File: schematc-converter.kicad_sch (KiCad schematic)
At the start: 52 parts, among them IC2 ACHS-7123-000E, IC3 LM5106MMX_NOPB, IC5 HCPL2531SDM, Q1 CSD19531Q5AT, Q2 CSD19531Q5AT

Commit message: Repair files
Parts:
- removed D2, D3, D4: LED, Diode_SMD:D_1206_3216Metric, symbol Device:LED
- removed R2, R3, R4: 1k, LED_SMD:LED_1206_3216Metric, symbol Device:R
- added C52: 100n, symbol Device:C
- added C53: 1n, symbol Device:C
- added IC2: ACHS-7123-000E, SOIC127P606X204-8N, symbol achs Current Hall Sensor:ACHS-7123-000E
- added R18: 10k, LED_SMD:LED_1206_3216Metric, symbol Device:R
- added R18: 20k, LED_SMD:LED_1206_3216Metric, symbol Device:R
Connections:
- net +5V: now also C52.1, IC2.8 (VDD)
- net GND: now also C52.2, C53.2, IC2.5 (GND), R18.1
- net SC+: now also IC2.1 (IP+_1), IC2.2 (IP+_2)
- net SC_c2: now also R18.2
- new net: IC2.7 (VOUT), R18.2
- new net: C53.1, IC2.6 (FILTER)
- new net MC+: IC2.3 (IP-_1), IC2.4 (IP-_2)
- new net MC_c: R18.1, R18.2
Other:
- note removed: "Signal diodes"
- moved on the sheet: C26, C37, C38, C39, C40, C41, C42, C43, C47, C48, D10, D8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

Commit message: P1
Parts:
- removed C49, C50: 15p, symbol Device:C
- removed C51: 100n, symbol Device:C
- removed IC5: HCPL2531SDM, HCPL2531SDM, symbol HCLP2530 transoptor:HCPL2531SDM
- removed R18 (x2): 10k, LED_SMD:LED_1206_3216Metric, symbol Device:R
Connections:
- net at IC3.7 (EN): now also R2.2
- net at IC3.8 (IN): now also R2.1
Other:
- note added: "Sprawdzic rezystory i wydajnosc ESP, pobor transoprtora i pobor drivera"
- note removed: "Sprawdzic rezystory i wydajnosc ESP, pobor transoprtora i pobor drivera Jakie bramki NOT?"
- moved on the sheet: R2

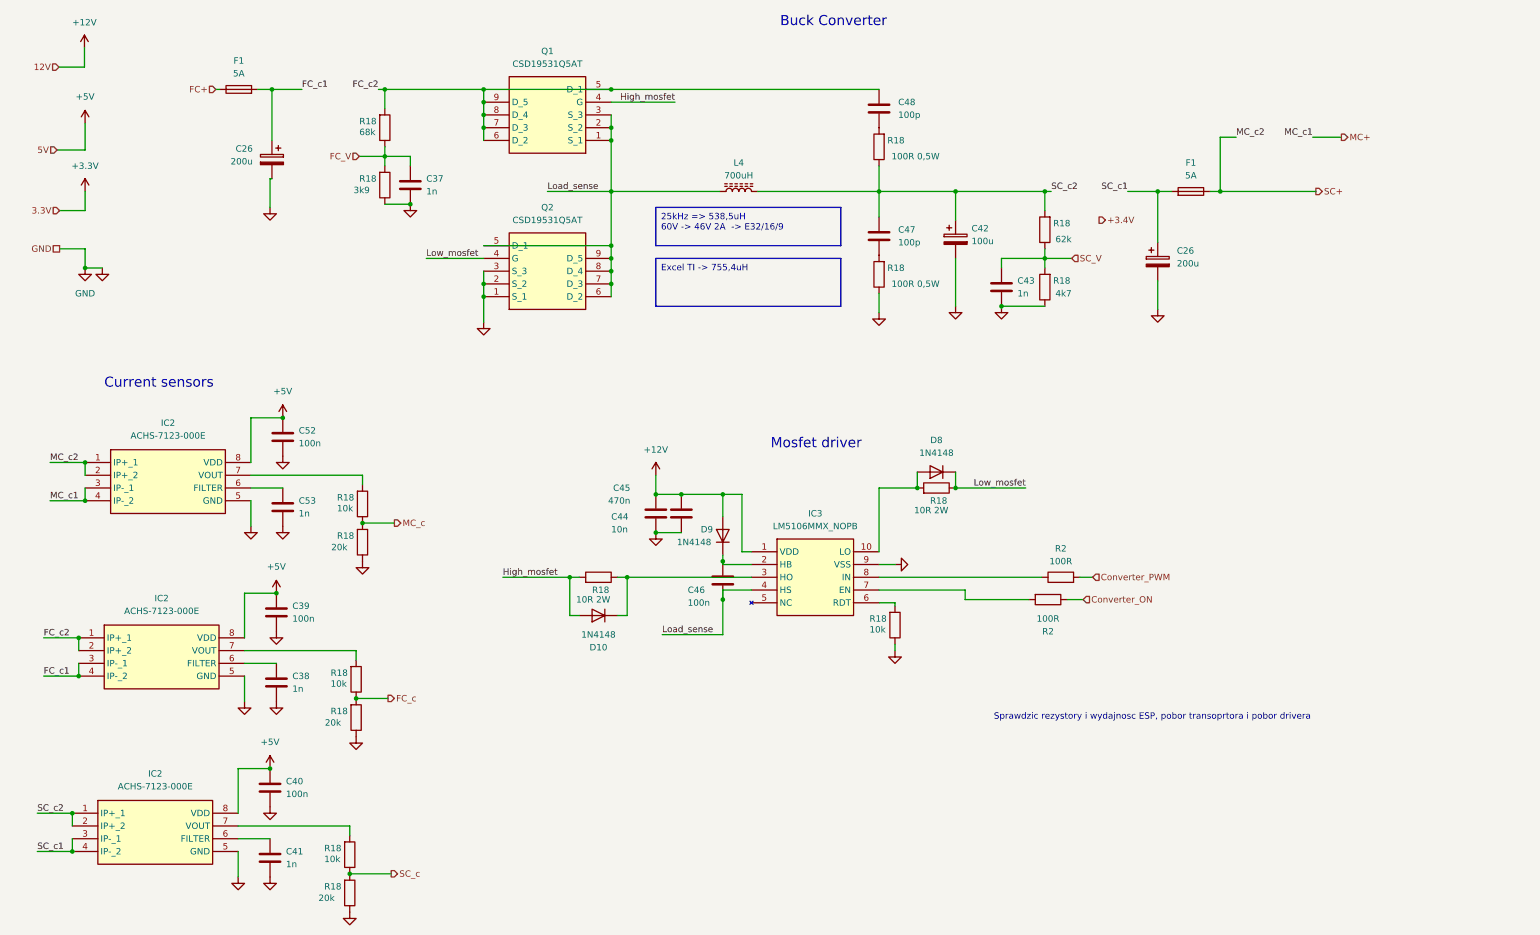
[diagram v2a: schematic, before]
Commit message: Add test points
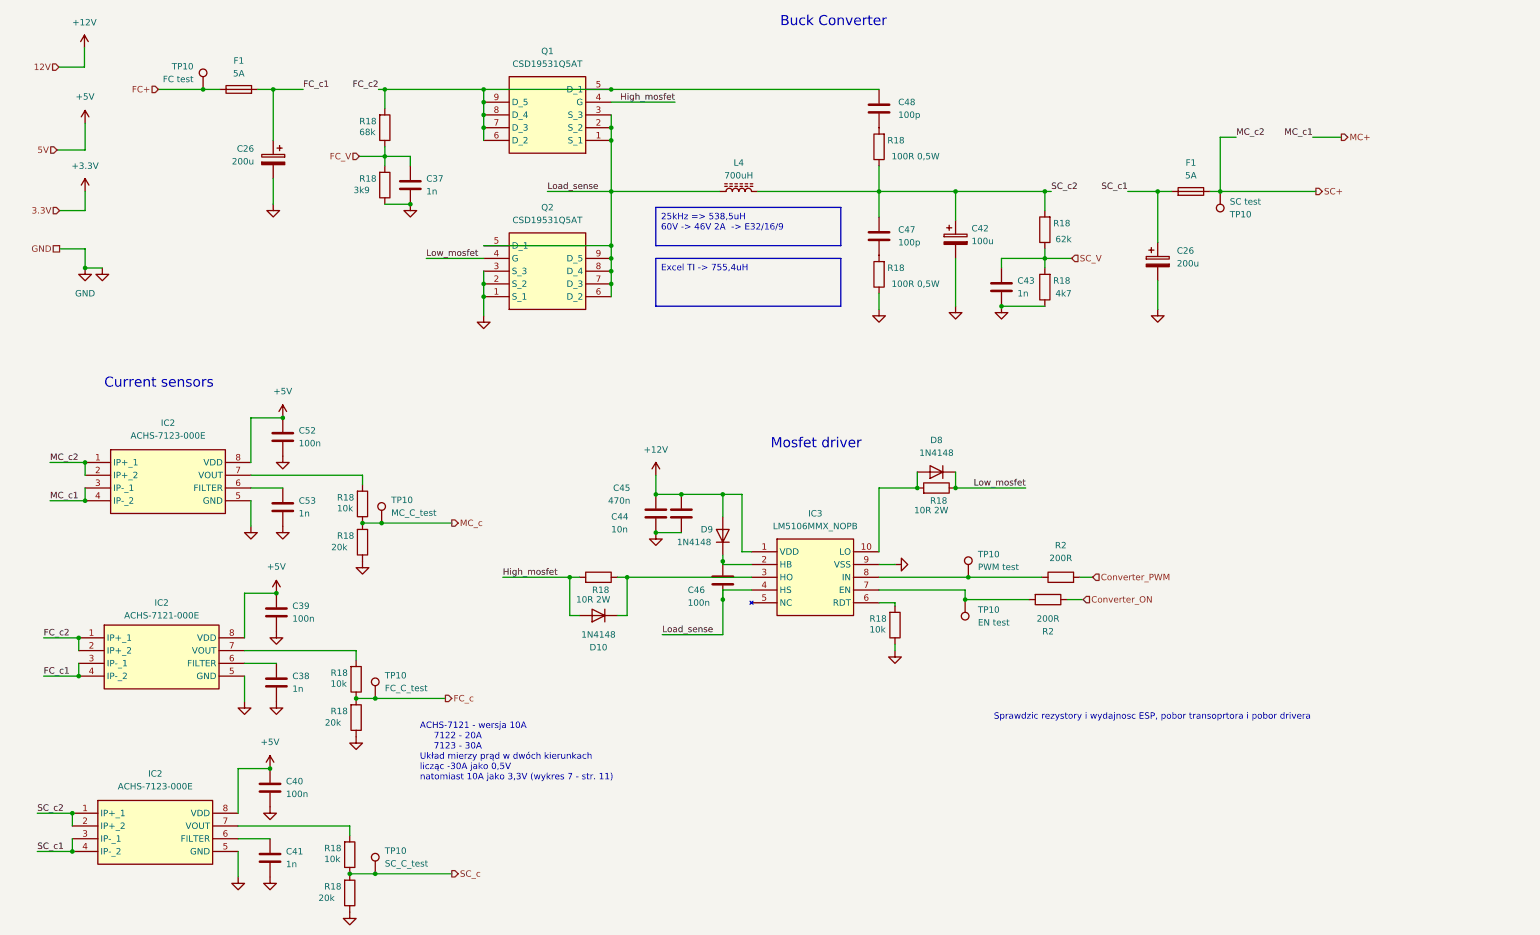
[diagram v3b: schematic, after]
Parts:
- added TP10: SC_C_test, symbol Connector:TestPoint
- added TP10: PWM test, symbol Connector:TestPoint
- added TP10: SC test, symbol Connector:TestPoint
- added TP10: EN test, symbol Connector:TestPoint
- added TP10: FC test, symbol Connector:TestPoint
- added TP10: MC_C_test, symbol Connector:TestPoint
- added TP10: FC_C_test, symbol Connector:TestPoint
- IC2: value ACHS-7123-000E -> ACHS-7121-000E
- R2: value 100R -> 200R
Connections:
- net FC+: now also TP10.1
- net FC_c: now also TP10.1
- net MC_c: now also TP10.1
- net SC+: now also TP10.1
- net SC_c: now also TP10.1
- net at IC3.7 (EN), R2.2: now also TP10.1
- net at IC3.8 (IN), R2.1: now also TP10.1
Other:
- note added: "ACHS-7121 - wersja 10A 7122 - 20A 7123 - 30A Układ mierzy prąd w dwóch kierunkach licząc -30A jako 0,5V natomiast 10A jako 3,3V (wykres 7 - str. 11)"

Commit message: Edit mosfets outputs
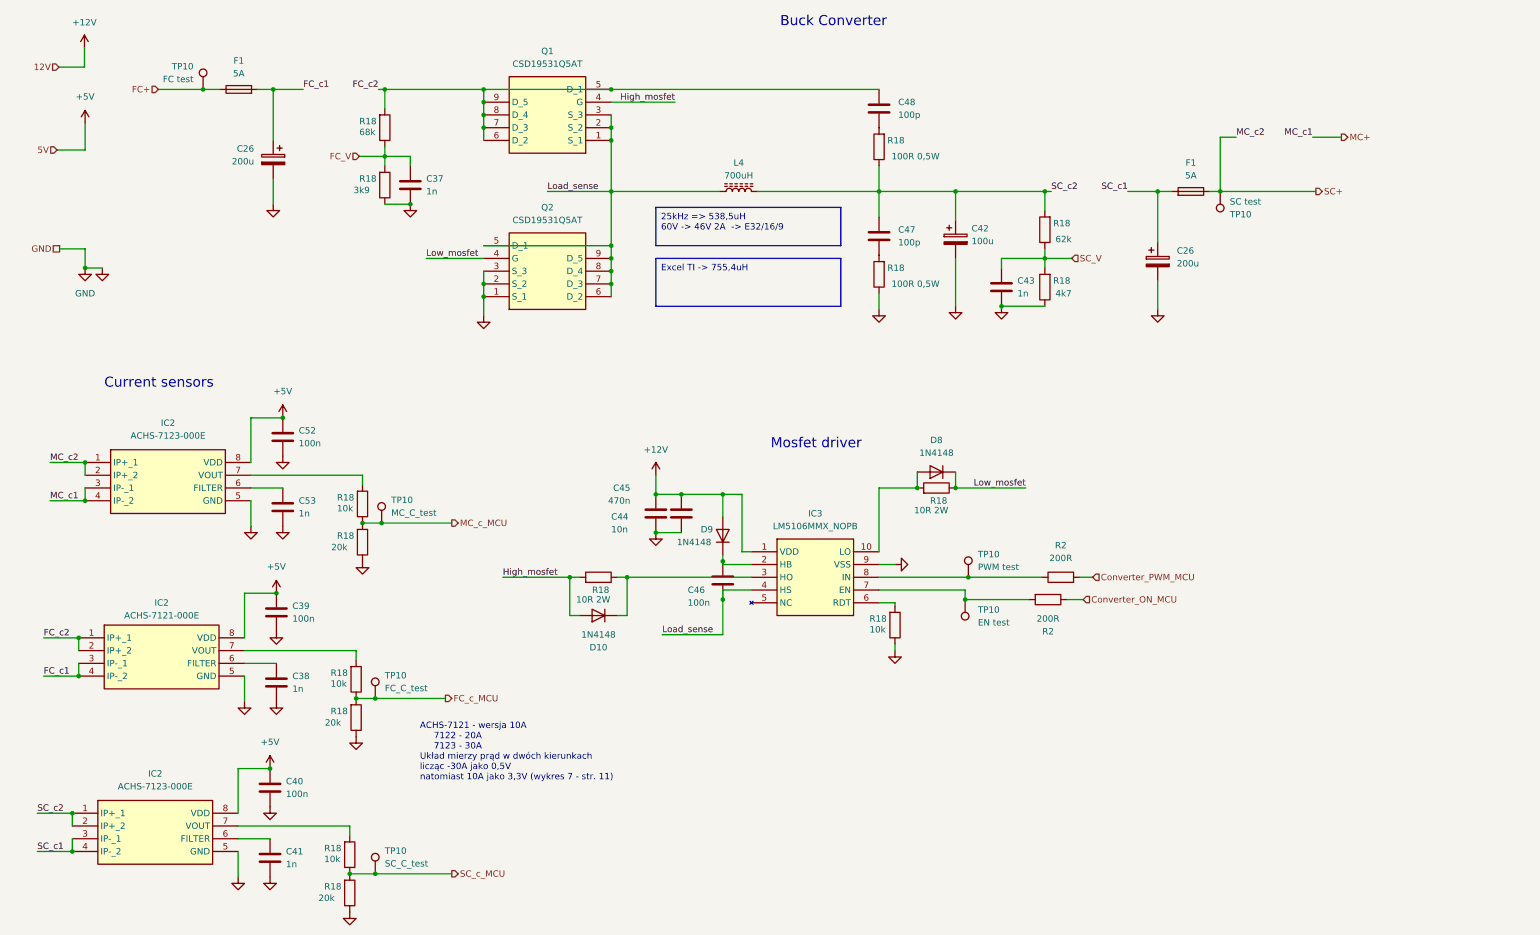
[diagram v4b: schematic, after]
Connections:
- net Converter_ON renamed Converter_ON_MCU
- net Converter_PWM renamed Converter_PWM_MCU
- net FC_c renamed FC_c_MCU
- net MC_c renamed MC_c_MCU
- net SC_c renamed SC_c_MCU
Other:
- note removed: "Sprawdzic rezystory i wydajnosc ESP, pobor transoprtora i pobor drivera"
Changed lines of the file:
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@@
-    (stroke (width 0) (type default))
-  )
-  (wire (pts (xy 21.59 53.975) (xy 26.67 53.975))
     (stroke (width 0) (type default))
   )
@@
   )
   (wire (pts (xy 86.36 43.18) (xy 86.36 45.085))
-    (stroke (width 0) (type default))
-  )
-  (wire (pts (xy 26.67 53.975) (xy 26.67 50.165))
     (stroke (width 0) (type default))
   )
@@
   (text "Current sensors\n" (at 30.48 89.535 0)
     (effects (font (size 2 2)) (justify left bottom))
-  )
-  (text "Sprawdzic rezystory i wydajnosc ESP, pobor transoprtora i pobor drivera\n"
-    (at 207.645 155.575 0)
-    (effects (font (size 1.27 1.27)) (justify left bottom))
   )
   (text "ACHS-7121 - wersja 10A\n     7122 - 20A\n     7123 - 30A\nUkład mierzy prąd w dwóch kierunkach \nlicząc -30A jako 0,5V\nnatomiast 10A jako 3,3V (wykres 7 - str. 11)"
@@
     (effects (font (size 1.27 1.27)) (justify right))
   )
-  (hierarchical_label "SC_c" (shape output) (at 99.695 186.055 0) (fields_autoplaced)
+  (hierarchical_label "SC_c_MCU" (shape output) (at 99.695 186.055 0) (fields_autoplaced)
     (effects (font (size 1.27 1.27)) (justify left))
   )
@@
     (effects (font (size 1.27 1.27)) (justify right))
   )
-  (hierarchical_label "3.3V" (shape input) (at 21.59 53.975 180) (fields_autoplaced)
-    (effects (font (size 1.27 1.27)) (justify right))
-  )
-  (hierarchical_label "MC_c" (shape output) (at 99.695 116.205 0) (fields_autoplaced)
+  (hierarchical_label "MC_c_MCU" (shape output) (at 99.695 116.205 0) (fields_autoplaced)
     (effects (font (size 1.27 1.27)) (justify left))
   )
@@
     (effects (font (size 1.27 1.27)) (justify right))
   )
-  (hierarchical_label "FC_c" (shape output) (at 98.425 151.13 0) (fields_autoplaced)
+  (hierarchical_label "FC_c_MCU" (shape output) (at 98.425 151.13 0) (fields_autoplaced)
     (effects (font (size 1.27 1.27)) (justify left))
   )
@@
     (effects (font (size 1.27 1.27)) (justify right))
   )
-  (hierarchical_label "Converter_ON" (shape input) (at 225.425 131.445 0) (fields_autoplaced)
+  (hierarchical_label "Converter_ON_MCU" (shape input) (at 225.425 131.445 0) (fields_autoplaced)
     (effects (font (size 1.27 1.27)) (justify left))
   )
-  (hierarchical_label "Converter_PWM" (shape input) (at 227.33 127 0) (fields_autoplaced)
+  (hierarchical_label "Converter_PWM_MCU" (shape input) (at 227.33 127 0) (fields_autoplaced)
     (effects (font (size 1.27 1.27)) (justify left))
   )
@@
         )
       )
-    )
-  )
-  (symbol (lib_id "power:+3.3V") (at 26.67 50.165 0) (unit 1)
-    (in_bom yes) (on_board yes) (dnp no) (fields_autoplaced)
-    (property "Reference" "#PWR07" (at 26.67 53.975 0)
-      (effects (font (size 1.27 1.27)) hide)
-    )
-    (property "Value" "+3.3V" (at 26.67 45.085 0)
-      (effects (font (size 1.27 1.27)))
-    )
-    (property "Footprint" "" (at 26.67 50.165 0)
-      (effects (font (size 1.27 1.27)) hide)
-    )
-    (property "Datasheet" "" (at 26.67 50.165 0)
-      (effects (font (size 1.27 1.27)) hide)
-    )
-    (pin "1")
-    (instances
-      (project "schematc-io"
-        (path "/9df92369-2505-4e62-b8bf-4ed31fcfe034"
-          (reference "#PWR07") (unit 1)
-        )
-      )
-      (project "schematic-main"
-        (path "/c9ad7189-d3b2-414a-9743-efd8e57cd755/f92f58ec-64e0-437c-bc00-8ae46a3b3054"
-          (reference "#PWR07") (unit 1)
-        )
-        (path "/c9ad7189-d3b2-414a-9743-efd8e57cd755/e4695f4d-6fa6-4597-a598-6a2f28a255eb"
-          (reference "#PWR036") (unit 1)
-        )
-        (path "/c9ad7189-d3b2-414a-9743-efd8e57cd755/8fa22090-ff4c-4c1d-88ea-3ea830fd1860"
-          (reference "#PWR0105") (unit 1)
-        )
-      )

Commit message: First pcb
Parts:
- removed C26 (x2): 200u, Capacitor_SMD:CP_Elec_8x10.5, symbol Device:C_Polarized
- added C26: 100u 100V, Capacitor_THT:CP_Radial_D10.0mm_P5.00mm, symbol Device:C_Polarized
- C33: renamed from C40; footprint (none) -> Capacitor_SMD:C_1206_3216Metric
- C34: renamed from C41; footprint (none) -> Capacitor_SMD:C_1206_3216Metric
- C35: renamed from C39; footprint (none) -> Capacitor_SMD:C_1206_3216Metric
- C36: renamed from C38; footprint (none) -> Capacitor_SMD:C_1206_3216Metric
- C37: renamed from C52; footprint (none) -> Capacitor_SMD:C_1206_3216Metric
- C38: renamed from C53; footprint (none) -> Capacitor_SMD:C_1206_3216Metric
- C39: renamed from C37; footprint (none) -> Capacitor_SMD:C_1206_3216Metric
- C40: renamed from C45; footprint (none) -> Capacitor_SMD:C_1206_3216Metric
- C41: renamed from C44; footprint (none) -> Capacitor_SMD:C_1206_3216Metric
- C42: renamed from C46; value 100n -> 100n 100V; footprint (none) -> Capacitor_SMD:C_1206_3216Metric
- C43: renamed from C48; value 100p -> 100p 100V; footprint (none) -> Capacitor_SMD:C_1206_3216Metric
- C44: renamed from C47; value 100p -> 100p 100V; footprint (none) -> Capacitor_SMD:C_1206_3216Metric
- C45: renamed from C42; value 100u -> 100u 100V; footprint (none) -> Capacitor_THT:CP_Radial_D10.0mm_P5.00mm; Field4 (none) -> Low ESR
- C46: renamed from C43; footprint (none) -> Capacitor_SMD:C_1206_3216Metric
- L3: renamed from L4; footprint (none) -> Inductor_THT_Wurth:L_Wurth_WE-HCFT-2012_LeadDiameter1.2mm
- TP10: footprint (none) -> Connector_PinSocket_2.54mm:PinSocket_1x01_P2.54mm_Vertical
- renumbered D10 to D7, D9 to D8, D8 to D9, IC3 to IC6, Q2 to Q1, Q1 to Q2
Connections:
- net FC_c1: now also C26.1
- net GND: now also C26.2
- net Load_sense renamed Bootstrap
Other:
- moved on the sheet: C45, C46, F1, R18, TP10

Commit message: Buck - boost converter
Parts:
- added C47: 470n, Capacitor_SMD:C_1206_3216Metric, symbol Device:C
- added C48: 10n, Capacitor_SMD:C_1206_3216Metric, symbol Device:C
- added C49: 100n 100V, Capacitor_SMD:C_1206_3216Metric, symbol Device:C
- added D10, D11, D12: 1N4148, Diode_THT:D_DO-35_SOD27_P7.62mm_Horizontal, symbol Diode:1N4148
- added IC7: LM5106MMX_NOPB, SOP50P490X110-10N, symbol lm5106 mmx:LM5106MMX_NOPB
- added Q3, Q4: CSD19531Q5AT, CSD19531Q5AT, symbol csd19531 q5at mosfet 100v:CSD19531Q5AT
- added R45, R47: 10R 2W, LED_SMD:LED_1206_3216Metric, symbol Device:R
- added R46: 10k, LED_SMD:LED_1206_3216Metric, symbol Device:R
- added R48, R49: 200R, LED_SMD:LED_1206_3216Metric, symbol Device:R
- added R50, R51: 0R, LED_SMD:LED_1206_3216Metric, symbol Device:R
- added TP21: EN test, Connector_PinSocket_2.54mm:PinSocket_1x01_P2.54mm_Vertical, symbol Connector:TestPoint
- added TP22: PWM test, Connector_PinSocket_2.54mm:PinSocket_1x01_P2.54mm_Vertical, symbol Connector:TestPoint
- renumbered C26 to C32, F1 to F2, TP10 to TP13, TP10 to TP14, TP10 to TP15, TP10 to TP16, TP10 to TP17, TP10 to TP18, TP10 to TP19
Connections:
- net +12V: now also C47.1, C48.1, D11.2 (A), IC7.1 (VDD)
- net FC_c2: now also R50.1
- net GND: now also C47.2, C48.2, IC7.9 (VSS), Q3.1 (S_1), Q3.2 (S_2), Q3.3 (S_3), R46.1
- net SC_c2: now also Q4.5 (D_1), Q4.6 (D_2), Q4.7 (D_3), Q4.8 (D_4), Q4.9 (D_5), R51.2; no longer C44.1, L3.2, R18.1
- net Bootstrap renamed Bootstrap_A
- net Bootstrap_A: now also R50.2
- net Converter_ON_MCU renamed Converter_ON_B_MCU
- net Converter_ON_B_MCU: now also R48.1
- net Converter_PWM_MCU renamed Converter_PWM_B_MCU
- net Converter_PWM_B_MCU: now also R49.2
- net High_mosfet renamed High_mosfet_A
- net Low_mosfet renamed Low_mosfet_A
- new net: IC7.7 (EN), R48.2, TP21.1
- new net: D12.2 (A), IC7.10 (LO), R47.2
- new net: C49.1, D11.1 (K), IC7.2 (HB)
- new net: D10.1 (K), IC7.3 (HO), R45.1
- new net: IC7.6 (RDT), R46.2
- new net: IC7.8 (IN), R49.1, TP22.1
- new net Bootstrap_B: C44.1, C49.2, IC7.4 (HS), L3.2, Q3.5 (D_1), Q3.6 (D_2), Q3.7 (D_3), Q3.8 (D_4), Q3.9 (D_5), Q4.1 (S_1), Q4.2 (S_2), Q4.3 (S_3), R18.1, R51.1
- new net High_mosfet_B: D10.2 (A), Q4.4 (G), R45.2
- new net Low_mosfet_B: D12.1 (K), Q3.4 (G), R47.1
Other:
- note added: "Mosfet driver A"
- note added: "Mosfet driver B"
- note removed: "Mosfet driver"
- moved on the sheet: C40, C41, C42, C43, C44, C45, C46, D7, D8, D9, F2, IC6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

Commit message: PCB design 50%
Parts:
- D10, D11, D12, D7, D8, D9: value 1N4148 -> SKL120-AQ; footprint Diode_THT:D_DO-35_SOD27_P7.62mm_Horizontal -> SODFL3718X170N
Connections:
- net MC+: now also IC2.1 (IP+_1), IC2.2 (IP+_2); no longer IC2.3 (IP-_1), IC2.4 (IP-_2)
- net SC+: now also IC2.3 (IP-_1), IC2.4 (IP-_2); no longer IC2.1 (IP+_1), IC2.2 (IP+_2)
- net SC_c1: now also C45.1, Q4.5 (D_1), Q4.6 (D_2), Q4.7 (D_3), Q4.8 (D_4), Q4.9 (D_5), R18.2, R51.2; no longer F2.2
- net SC_c2: now also F2.2; no longer C45.1, Q4.5 (D_1), Q4.6 (D_2), Q4.7 (D_3), Q4.8 (D_4), Q4.9 (D_5), R18.2, R51.2
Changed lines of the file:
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@@
 	)
 	(label "SC_c1"
-		(at 243.84 33.02 180)
+		(at 228.6 33.02 0)
 		(fields_autoplaced yes)
 		(effects
@@
 				(size 1.27 1.27)
 			)
-			(justify right bottom)
+			(justify left bottom)
 		)
 	)
@@
 	)
 	(label "MC_c2"
-		(at 259.715 22.225 0)
+		(at 274.955 22.225 180)
 		(fields_autoplaced yes)
 		(effects
@@
 				(size 1.27 1.27)
 			)
-			(justify left bottom)
+			(justify right bottom)
 		)
 	)
 	(label "MC_c1"
-		(at 274.955 22.225 180)
+		(at 259.715 22.225 0)
 		(fields_autoplaced yes)
 		(effects
@@
 				(size 1.27 1.27)
 			)
-			(justify right bottom)
+			(justify left bottom)
 		)
 	)
@@
 	)
 	(label "SC_c2"
-		(at 228.6 33.02 0)
+		(at 243.84 33.02 180)
 		(fields_autoplaced yes)
 		(effects
@@
 				(size 1.27 1.27)
 			)
-			(justify left bottom)
+			(justify right bottom)
 		)
 	)
@@
 			)
 		)
-		(property "Value" "1N4148"
+		(property "Value" "SKL120-AQ"
 			(at 229.87 131.445 0)
 			(effects
@@
 			)
 		)
-		(property "Footprint" "Diode_THT:D_DO-35_SOD27_P7.62mm_Horizontal"
+		(property "Footprint" "SODFL3718X170N"
 			(at 229.87 135.255 0)
 			(effects
@@
 			)
 		)
-		(property "Value" "1N4148"
+		(property "Value" "SKL120-AQ"
 			(at 157.48 163.83 0)
 			(effects
@@
 			)
 		)
-		(property "Footprint" "Diode_THT:D_DO-35_SOD27_P7.62mm_Horizontal"
+		(property "Footprint" "SODFL3718X170N"
 			(at 157.48 160.02 0)
 			(effects
@@
 			)
 		)
-		(property "Value" "1N4148"
+		(property "Value" "SKL120-AQ"
 			(at 227.33 83.82 0)
 			(effects
@@
 			)
 		)
-		(property "Footprint" "Diode_THT:D_DO-35_SOD27_P7.62mm_Horizontal"
+		(property "Footprint" "SODFL3718X170N"
 			(at 227.33 87.63 0)
 			(effects
@@
 			)
 		)
-		(property "Value" "1N4148"
+		(property "Value" "SKL120-AQ"
 			(at 158.75 116.84 0)
 			(effects
@@
 			)
 		)
-		(property "Footprint" "Diode_THT:D_DO-35_SOD27_P7.62mm_Horizontal"
+		(property "Footprint" "SODFL3718X170N"
 			(at 158.75 113.03 0)
 			(effects
@@
 			)
 		)
-		(property "Value" "1N4148"
+		(property "Value" "SKL120-AQ"
 			(at 177.8 98.425 90)
 			(effects
@@
 			)
 		)
-		(property "Footprint" "Diode_THT:D_DO-35_SOD27_P7.62mm_Horizontal"
+		(property "Footprint" "SODFL3718X170N"
 			(at 183.515 97.155 0)
 			(effects
@@
 			)
 		)
-		(property "Value" "1N4148"
+		(property "Value" "SKL120-AQ"
 			(at 176.53 145.415 90)
 			(effects
@@
 			)
 		)
-		(property "Footprint" "Diode_THT:D_DO-35_SOD27_P7.62mm_Horizontal"
+		(property "Footprint" "SODFL3718X170N"
 			(at 182.245 144.145 0)
 			(effects
